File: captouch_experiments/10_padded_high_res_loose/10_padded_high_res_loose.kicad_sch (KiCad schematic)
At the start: 3 parts, among them J1 Conn_01x08_Male, J2 Conn_01x32_Male, U1 captouch_8x32_grid

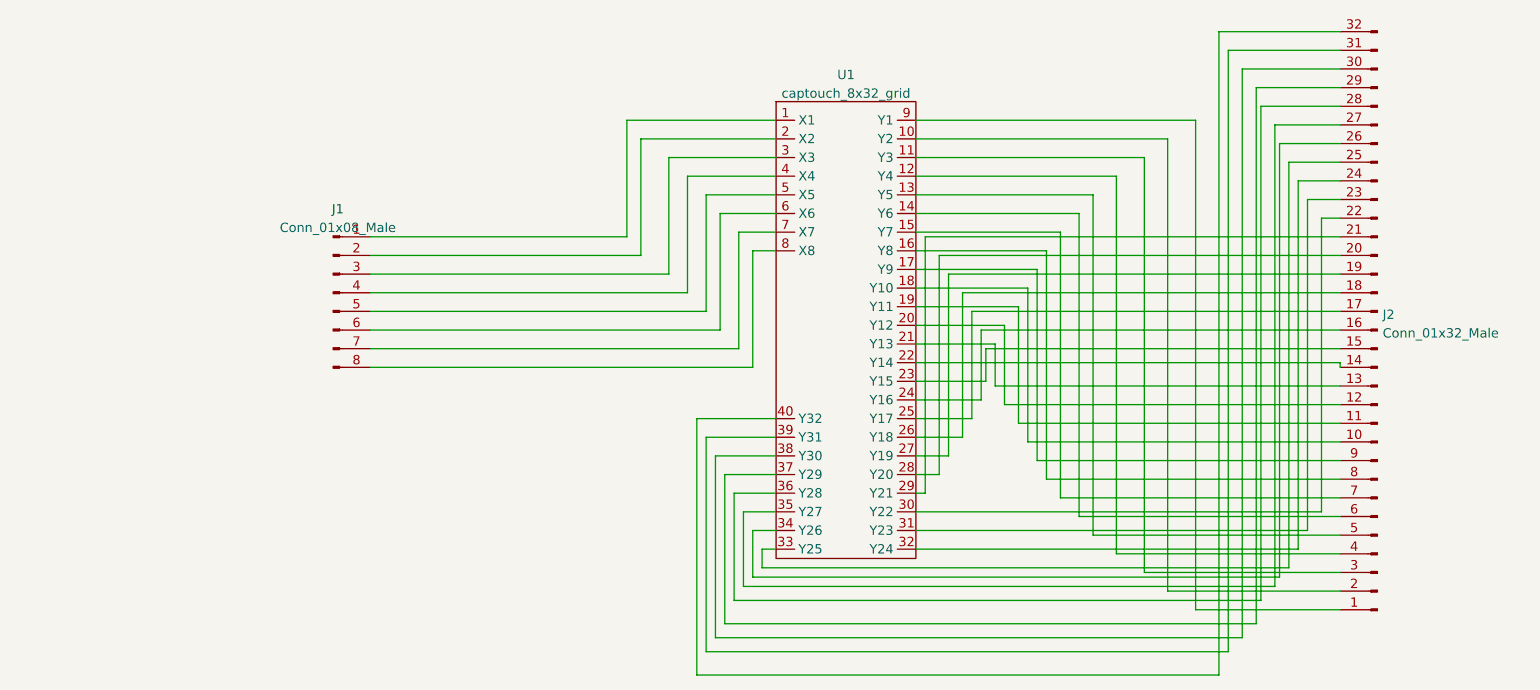
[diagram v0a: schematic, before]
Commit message: added new high resolution touch boards
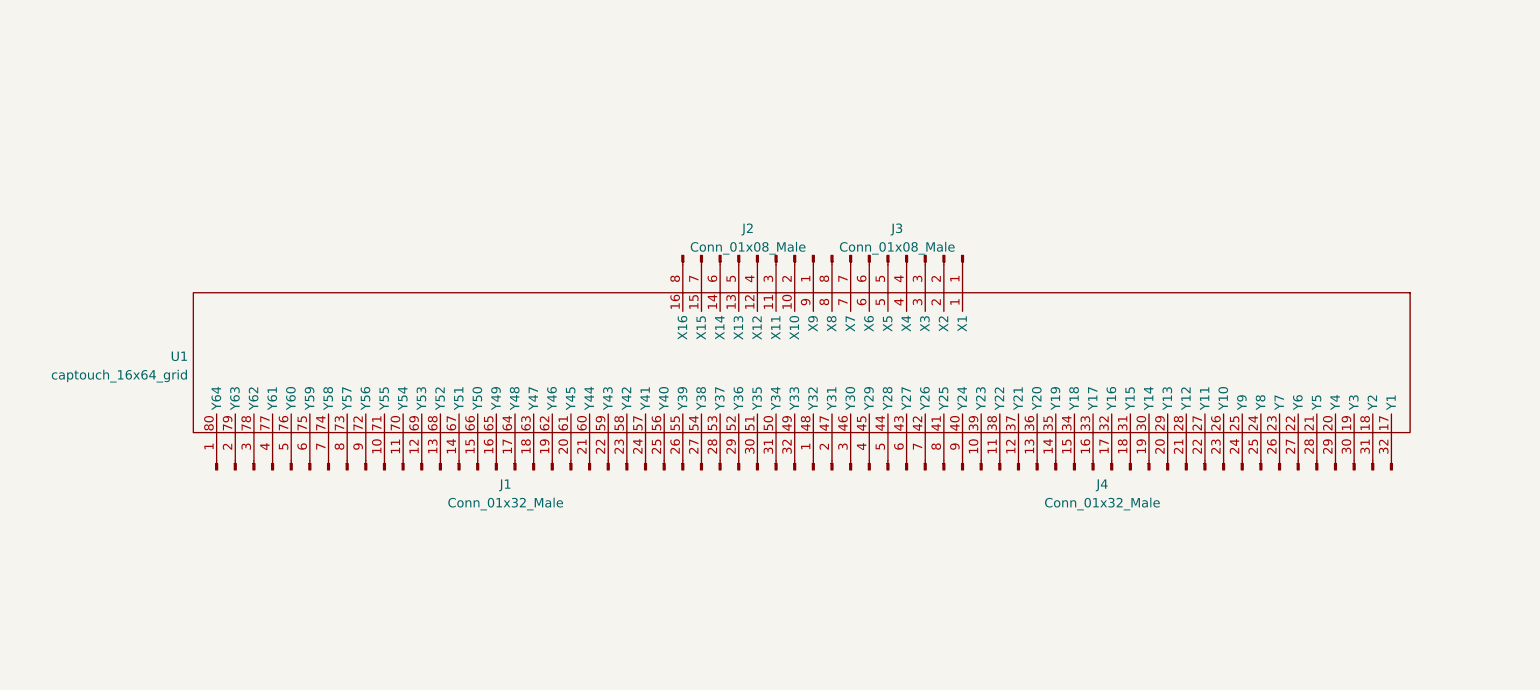
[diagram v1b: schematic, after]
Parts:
- removed U1: captouch_8x32_grid, ASMR_footprints:captouch_8x32_diamond_baseline, symbol asmr-kicad:captouch_8x32_grid
- added J1: Conn_01x32_Male, ASMR_footprints:Conn_FFC_1x32_0.5mm_Molex_5019513210, symbol Connector:Conn_01x32_Male
- added J2: Conn_01x08_Male, ASMR_footprints:Conn_FFC_1x8_0.5mm_Molex_5019510830, symbol Connector:Conn_01x08_Male
- added U1: captouch_16x64_grid, ASMR_footprints:captouch_16x64_padded_interleaved_loose, symbol asmr-kicad:captouch_16x64_grid
- renumbered J1 to J3, J2 to J4
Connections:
- net at J3.1 (Pin_1): now also U1.1 (X1)
- net at J3.2 (Pin_2): now also U1.2 (X2)
- net at J3.3 (Pin_3): now also U1.3 (X3)
- net at J3.4 (Pin_4): now also U1.4 (X4)
- net at J3.5 (Pin_5): now also U1.5 (X5)
- net at J3.6 (Pin_6): now also U1.6 (X6)
- net at J3.7 (Pin_7): now also U1.7 (X7)
- net at J3.8 (Pin_8): now also U1.8 (X8)
- net at J4.1 (Pin_1): now also U1.48 (Y32)
- net at J4.10 (Pin_10): now also U1.39 (Y23)
- net at J4.11 (Pin_11): now also U1.38 (Y22)
- net at J4.12 (Pin_12): now also U1.37 (Y21)
- net at J4.13 (Pin_13): now also U1.36 (Y20)
- net at J4.14 (Pin_14): now also U1.35 (Y19)
- net at J4.15 (Pin_15): now also U1.34 (Y18)
- net at J4.16 (Pin_16): now also U1.33 (Y17)
- net at J4.17 (Pin_17): now also U1.32 (Y16)
- net at J4.18 (Pin_18): now also U1.31 (Y15)
- net at J4.19 (Pin_19): now also U1.30 (Y14)
- net at J4.2 (Pin_2): now also U1.47 (Y31)
- net at J4.20 (Pin_20): now also U1.29 (Y13)
- net at J4.21 (Pin_21): now also U1.28 (Y12)
- net at J4.22 (Pin_22): now also U1.27 (Y11)
- net at J4.23 (Pin_23): now also U1.26 (Y10)
- net at J4.24 (Pin_24): now also U1.25 (Y9)
- net at J4.25 (Pin_25): now also U1.24 (Y8)
- net at J4.26 (Pin_26): now also U1.23 (Y7)
- net at J4.27 (Pin_27): now also U1.22 (Y6)
- net at J4.28 (Pin_28): now also U1.21 (Y5)
- net at J4.29 (Pin_29): now also U1.20 (Y4)
- net at J4.3 (Pin_3): now also U1.46 (Y30)
- net at J4.30 (Pin_30): now also U1.19 (Y3)
- net at J4.31 (Pin_31): now also U1.18 (Y2)
- net at J4.32 (Pin_32): now also U1.17 (Y1)
- net at J4.4 (Pin_4): now also U1.45 (Y29)
- net at J4.5 (Pin_5): now also U1.44 (Y28)
- net at J4.6 (Pin_6): now also U1.43 (Y27)
- net at J4.7 (Pin_7): now also U1.42 (Y26)
- net at J4.8 (Pin_8): now also U1.41 (Y25)
- net at J4.9 (Pin_9): now also U1.40 (Y24)
- new net: J2.2 (Pin_2), U1.10 (X10)
- new net: J2.3 (Pin_3), U1.11 (X11)
- new net: J2.4 (Pin_4), U1.12 (X12)
- new net: J2.5 (Pin_5), U1.13 (X13)
- new net: J2.6 (Pin_6), U1.14 (X14)
- new net: J2.7 (Pin_7), U1.15 (X15)
- new net: J2.8 (Pin_8), U1.16 (X16)
- new net: J1.32 (Pin_32), U1.49 (Y33)
- new net: J1.31 (Pin_31), U1.50 (Y34)
- new net: J1.30 (Pin_30), U1.51 (Y35)
- new net: J1.29 (Pin_29), U1.52 (Y36)
- new net: J1.28 (Pin_28), U1.53 (Y37)
- new net: J1.27 (Pin_27), U1.54 (Y38)
- new net: J1.26 (Pin_26), U1.55 (Y39)
- new net: J1.25 (Pin_25), U1.56 (Y40)
- new net: J1.24 (Pin_24), U1.57 (Y41)
- new net: J1.23 (Pin_23), U1.58 (Y42)
- new net: J1.22 (Pin_22), U1.59 (Y43)
- new net: J1.21 (Pin_21), U1.60 (Y44)
- new net: J1.20 (Pin_20), U1.61 (Y45)
- new net: J1.19 (Pin_19), U1.62 (Y46)
- new net: J1.18 (Pin_18), U1.63 (Y47)
- new net: J1.17 (Pin_17), U1.64 (Y48)
- new net: J1.16 (Pin_16), U1.65 (Y49)
- new net: J1.15 (Pin_15), U1.66 (Y50)
- new net: J1.14 (Pin_14), U1.67 (Y51)
- new net: J1.13 (Pin_13), U1.68 (Y52)
- new net: J1.12 (Pin_12), U1.69 (Y53)
- new net: J1.11 (Pin_11), U1.70 (Y54)
- new net: J1.10 (Pin_10), U1.71 (Y55)
- new net: J1.9 (Pin_9), U1.72 (Y56)
- new net: J1.8 (Pin_8), U1.73 (Y57)
- new net: J1.7 (Pin_7), U1.74 (Y58)
- new net: J1.6 (Pin_6), U1.75 (Y59)
- new net: J1.5 (Pin_5), U1.76 (Y60)
- new net: J1.4 (Pin_4), U1.77 (Y61)
- new net: J1.3 (Pin_3), U1.78 (Y62)
- new net: J1.2 (Pin_2), U1.79 (Y63)
- new net: J1.1 (Pin_1), U1.80 (Y64)
- new net: J2.1 (Pin_1), U1.9 (X9)
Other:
- moved on the sheet: J3, J4
